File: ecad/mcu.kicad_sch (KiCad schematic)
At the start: 0 parts

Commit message: stuff
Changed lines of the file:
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@@
+		)
+	)
+	(hierarchical_label "VCA_Vref"
+		(shape output)
+		(at 52.07 82.55 0)
+		(effects
+			(font
+				(size 1.27 1.27)
+			)
+			(justify left)
 		)
 	)

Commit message: commiting before updating kicad
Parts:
- added U1: AD5686R, Package_SO:TSSOP-16_4.4x5mm_P0.65mm, symbol Analog_DAC:AD5686R
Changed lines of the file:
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@@
+		)
+	)
+	(symbol
+		(lib_id "Analog_DAC:AD5686R")
+		(at 114.3 82.55 0)
+		(unit 1)
+		(body_style 1)
+		(exclude_from_sim no)
+		(in_bom yes)
+		(on_board yes)
+		(in_pos_files yes)
+		(dnp no)
+		(fields_autoplaced yes)
+		(property "Reference" "U1"
+			(at 116.4433 101.6 0)
+			(show_name no)
+			(do_not_autoplace no)
+			(effects
+				(font
+					(size 1.27 1.27)
+				)
+				(justify left)
+			)
+		)
+		(property "Value" "AD5686R"
+			(at 116.4433 104.14 0)
+			(show_name no)
+			(do_not_autoplace no)
+			(effects
+				(font
+					(size 1.27 1.27)
+				)
+				(justify left)
+			)
+		)
+		(property "Footprint" "Package_SO:TSSOP-16_4.4x5mm_P0.65mm"
+			(at 114.3 113.284 0)
+			(hide yes)
+			(show_name no)
+			(do_not_autoplace no)
+			(effects
+				(font
+					(size 1.27 1.27)
+				)
+			)
+		)
+		(property "Datasheet" "https://www.analog.com/media/en/technical-documentation/data-sheets/ad5686r_5685r_5684r.pdf"
+			(at 114.3 117.602 0)
+			(hide yes)
+			(show_name no)
+			(do_not_autoplace no)
+			(effects
+				(font
+					(size 1.27 1.27)
+				)
+			)
+		)
+		(property "Description" "Quad, 16-/14-/12-Bit nanoDAC+ with 2 ppm/°C Reference, SPI Interface"
+			(at 114.3 115.316 0)
+			(hide yes)
+			(show_name no)
+			(do_not_autoplace no)
+			(effects
+				(font
+					(size 1.27 1.27)
+				)
+			)
+		)
+		(pin "16"
+		)
+		(pin "15"
+		)
+		(pin "4"
+		)
+		(pin "5"
+		)
+		(pin "6"
+		)
+		(pin "7"
+		)
+		(pin "8"
+		)
+		(pin "9"
+		)
+		(pin "10"
+		)
+		(pin "11"
+		)
+		(pin "12"
+		)
+		(pin "13"
+		)
+		(pin "14"
+		)
+		(pin "2"
+		)
+		(pin "3"
+		)
+		(pin "1"
+		)
+		(instances
+			(project "afm"
+				(path "/62de9aa8-4539-4ecb-8acc-2c7a46b3005b/609e7c1b-9183-4cd7-8dc2-8610036ea669"
+					(reference "U1")
+					(unit 1)
+				)
+			)
 		)
 	)

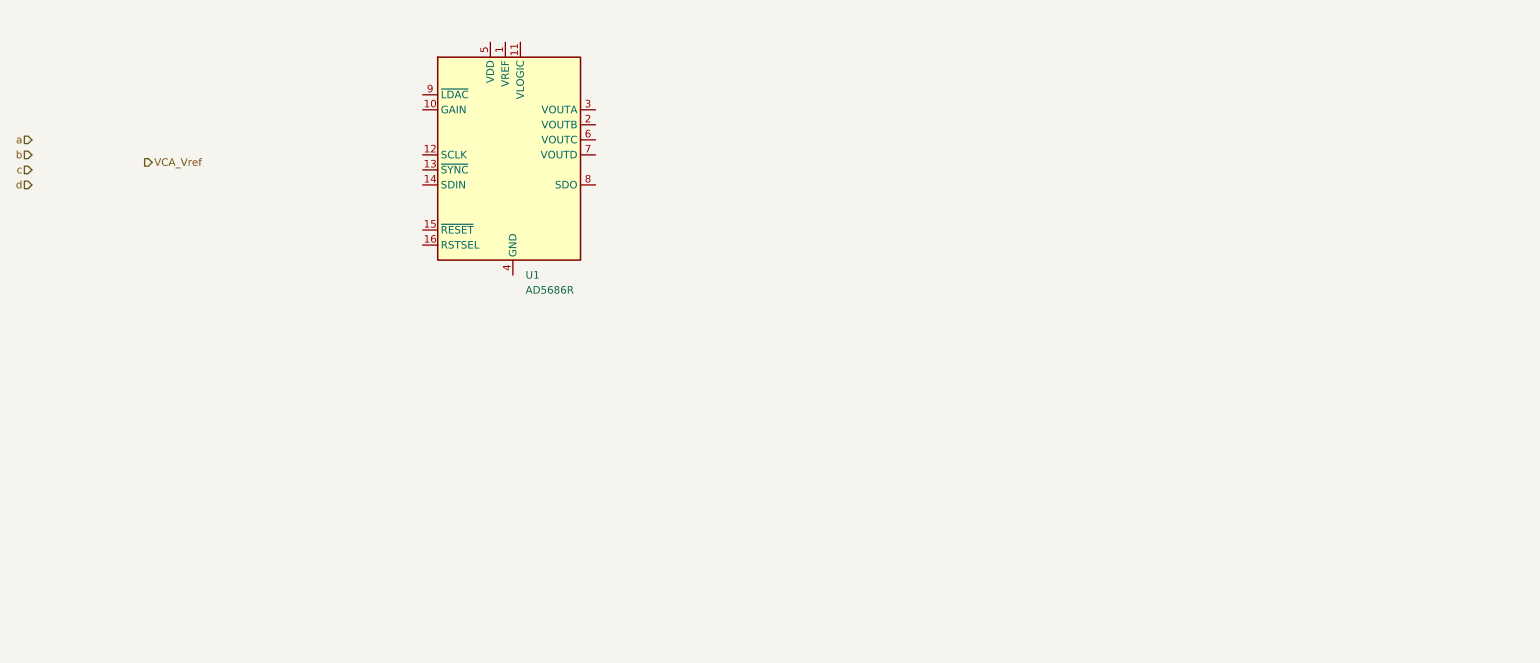
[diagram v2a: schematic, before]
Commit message: reorg; dac symbols
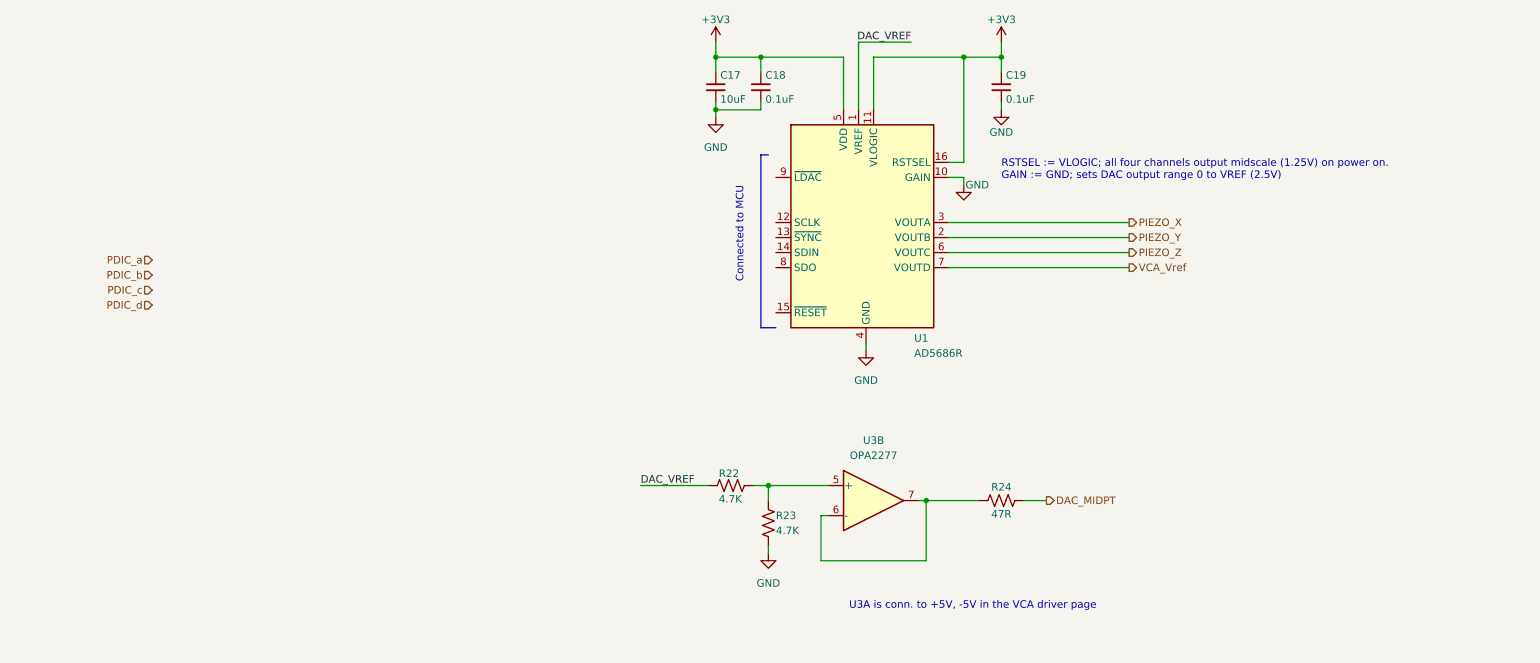
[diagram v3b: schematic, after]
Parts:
- removed U1: AD5686R, Package_SO:TSSOP-16_4.4x5mm_P0.65mm, symbol Analog_DAC:AD5686R
- added C17: 10uF, Package_SO:TSSOP-16_4.4x5mm_P0.65mm, symbol Device:C_Small
- added C18, C19: 0.1uF, Package_SO:TSSOP-16_4.4x5mm_P0.65mm, symbol Device:C_Small
- added R22, R23: 4.7K, symbol Device:R_US
- added R24: 47R, symbol Device:R_US
- added U1: AD5686R, Package_SO:TSSOP-16_4.4x5mm_P0.65mm, symbol AFM_Lib:AD5686R
- added U3: OPA2277, symbol Amplifier_Operational:OPA2277
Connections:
- net VCA_Vref: now also U1.7 (VOUTD)
- new net: R24.1, U3.6 (-), U3.7
- new net: R22.2, R23.1, U3.5 (+)
- new net +3V3: C17.1, C18.1, C19.1, U1.11 (VLOGIC), U1.16 (RSTSEL), U1.5 (VDD)
- new net DAC_MIDPT: R24.2
- new net DAC_VREF: R22.1, U1.1 (VREF)
- new net GND: C17.2, C18.2, C19.2, R23.2, U1.10 (GAIN), U1.4 (GND)
- new net PIEZO_X: U1.3 (VOUTA)
- new net PIEZO_Y: U1.2 (VOUTB)
- new net PIEZO_Z: U1.6 (VOUTC)
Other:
- note added: "Connected to MCU"
- note added: "RSTSEL := VLOGIC; all four channels output midscale (1.25V) on power on. GAIN := GND; sets DAC output range 0 to VREF (2.5V)"
- note added: "U3A is conn. to +5V, -5V in the VCA driver page"

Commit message: vca drv ref
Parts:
- removed U3: OPA2277, symbol Amplifier_Operational:OPA2277
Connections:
- net DAC_MIDPT renamed DAC_MID_Vref
- net VCA_Vref renamed VCA_DRV
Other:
- note added: "opa2277 here"
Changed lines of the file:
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@@
+		)
+	)
+	(text "opa2277 here"
+		(exclude_from_sim no)
+		(at 174.244 140.462 0)
+		(effects
+			(font
+				(size 1.27 1.27)
+			)
 		)
 	)
@@
 		)
 	)
-	(hierarchical_label "VCA_Vref"
+	(hierarchical_label "VCA_DRV"
 		(shape output)
 		(at 218.44 100.33 0)
@@
 		)
 	)
-	(hierarchical_label "DAC_MIDPT"
+	(hierarchical_label "DAC_MID_Vref"
 		(shape output)
 		(at 204.47 139.7 0)
@@
 				)
 			)
-		)
-	)
-	(symbol
-		(lib_id "Amplifier_Operational:OPA2277")
-		(at 175.26 139.7 0)
-		(unit 2)
-		(body_style 1)
-		(exclude_from_sim no)
-		(in_bom yes)
-		(on_board yes)
-		(in_pos_files yes)
-		(dnp no)
-		(fields_autoplaced yes)
-		(property "Reference" "U3"
-			(at 175.26 129.54 0)
-			(show_name no)
-			(do_not_autoplace no)
-			(effects
-				(font
-					(size 1.27 1.27)
-				)
-			)
-		)
-		(property "Value" "OPA2277"
-			(at 175.26 132.08 0)
-			(show_name no)
-			(do_not_autoplace no)
-			(effects
-				(font
-					(size 1.27 1.27)
-				)
-			)
-		)
-		(property "Footprint" ""
-			(at 175.26 139.7 0)
-			(hide yes)
-			(show_name no)
-			(do_not_autoplace no)
-			(effects
-				(font
-					(size 1.27 1.27)
-				)
-			)
-		)
-		(property "Datasheet" "https://www.ti.com/lit/ds/symlink/opa2277.pdf"
-			(at 175.26 139.7 0)
-			(hide yes)
-			(show_name no)
-			(do_not_autoplace no)
-			(effects
-				(font
-					(size 1.27 1.27)
-				)
-			)
-		)
-		(property "Description" "Dual High Precision Operational Amplifiers, DIP-8/SOIC-8"
-			(at 175.26 139.7 0)
-			(hide yes)
-			(show_name no)
-			(do_not_autoplace no)
-			(effects
-				(font
-					(size 1.27 1.27)
-				)
-			)
-		)
-		(pin "8"
-		)
-		(pin "4"
-		)
-		(pin "6"
-		)
-		(pin "5"
-		)
-		(pin "7"
-		)
-		(pin "3"
-		)
-		(pin "1"
-		)
-		(pin "2"
-		)
-		(instances
-			(project "afm"
-				(path "/62de9aa8-4539-4ecb-8acc-2c7a46b3005b/609e7c1b-9183-4cd7-8dc2-8610036ea669"
-					(reference "U3")
-					(unit 2)
-				)
-			)

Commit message: need to sweep
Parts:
- added C20, C21: 0.1uF, Package_SO:TSSOP-16_4.4x5mm_P0.65mm, symbol Device:C_Small
- added U6: OPA2277, symbol Amplifier_Operational:OPA2277
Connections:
- net GND: now also C20.2, C21.2
- net at R24.1: now also U6.1, U6.2 (-)
- net at R22.2, R23.1: now also U6.3 (+)
- new net +5V: C20.1, U6.8 (V+)
- new net -5V: C21.1, U6.4 (V-)
- no-connect marks 0 -> 3
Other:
- note removed: "opa2277 here"
